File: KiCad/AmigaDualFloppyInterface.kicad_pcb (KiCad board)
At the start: 2 copper layers, 62 x 69 mm, 21 parts, among them J1 Floppy Power In, J2 Floppy B, J3 Motherboard, J4 Floppy Power Out, J5 Floppy A, J6 Conn_01x02_Pin, J7 Conn_01x02_Pin, U1 74LS38, U2 74LS74, U3 74LS157

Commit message: Fix project footprint library
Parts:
- removed the OSHW at (60.0, 128.0)
- added OSHW: LOGO, MyFootprints:OSHW_logo, F.Cu at (60.0, 128.0)

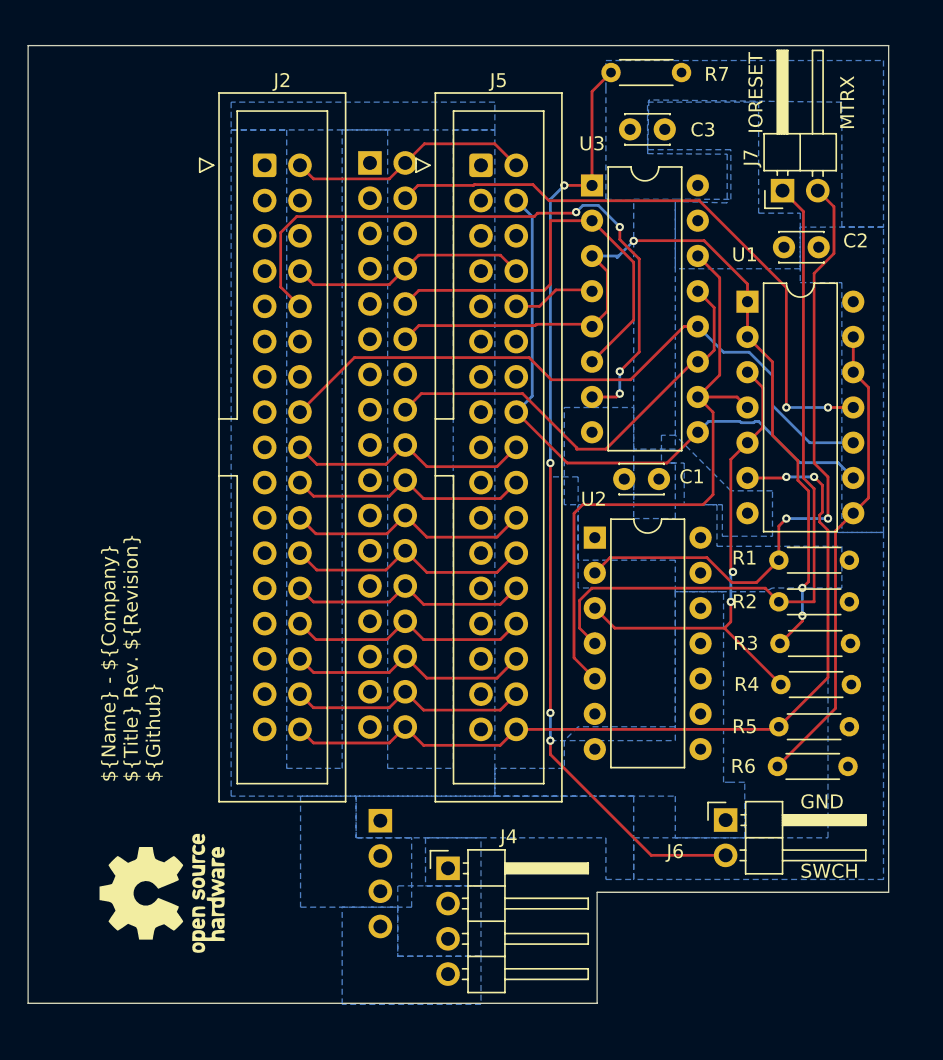
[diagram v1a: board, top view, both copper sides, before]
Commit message: Add files via upload
Updated design with separate df1 LED
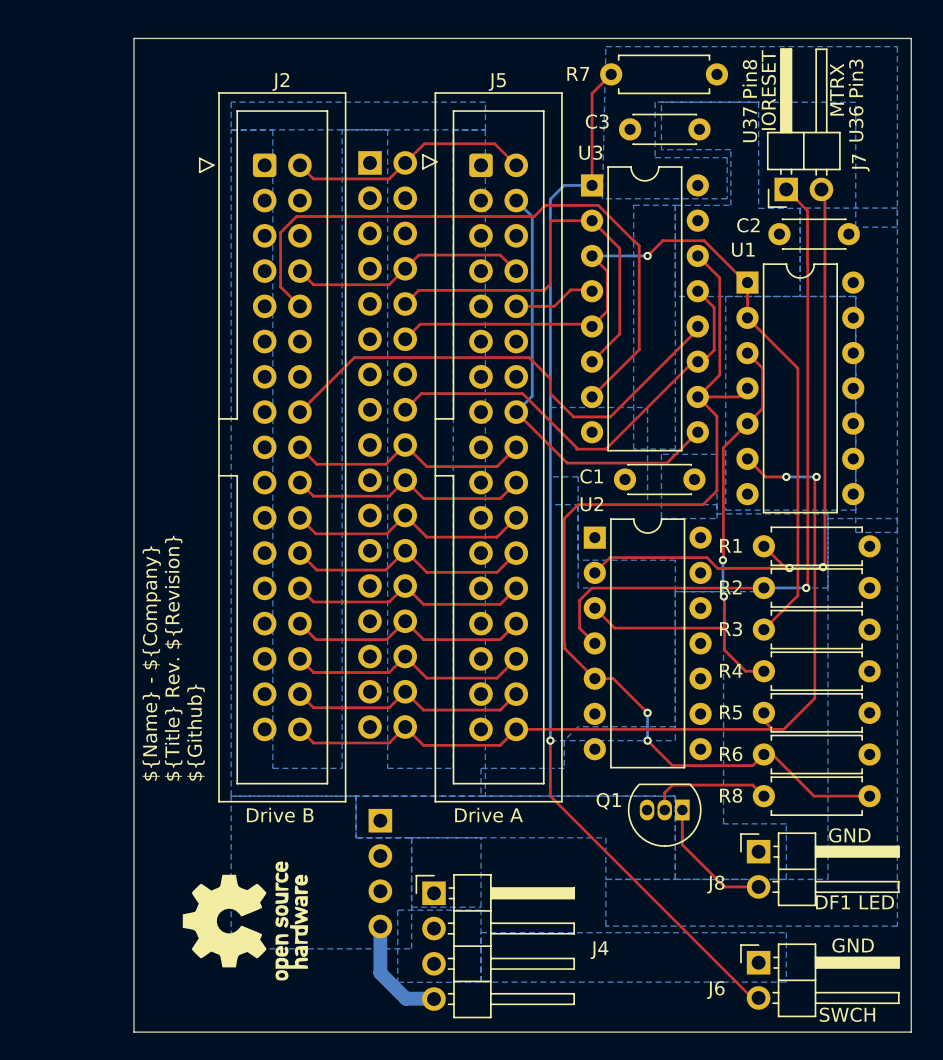
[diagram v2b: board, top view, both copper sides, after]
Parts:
- added J8: DF1 Activity, Connector_PinHeader_2.54mm:PinHeader_1x02_P2.54mm_Horizontal, F.Cu at (103.0, 125.0)
- added Q1: 2N3906, Package_TO_SOT_THT:TO-92_Inline, F.Cu at (97.5, 122.0)
- added R8: 4.7k, Resistor_THT:R_Axial_DIN0207_L6.3mm_D2.5mm_P7.62mm_Horizontal, F.Cu at (111.0, 121.0)
- C1, C2, C3: footprint Capacitor_THT:C_Disc_D3.0mm_W2.0mm_P2.50mm -> Capacitor_THT:C_Disc_D4.3mm_W1.9mm_P5.00mm
- J6: value Conn_01x02_Pin -> Drive Switch
- R1, R2, R3, R4, R5, R7: footprint Resistor_THT:R_Axial_DIN0204_L3.6mm_D1.6mm_P5.08mm_Horizontal -> Resistor_THT:R_Axial_DIN0207_L6.3mm_D2.5mm_P7.62mm_Horizontal
- R6: value 1k -> 10k; footprint Resistor_THT:R_Axial_DIN0204_L3.6mm_D1.6mm_P5.08mm_Horizontal -> Resistor_THT:R_Axial_DIN0207_L6.3mm_D2.5mm_P7.62mm_Horizontal
- moved J6 10.5 mm to (103.0, 133.0)
- moved OSHW 6.32 mm to (66.0, 130.0)
- moved C1 2.56 mm to (98.4, 98.2)
- moved R7 2.56 mm to (100.0, 69.0)
- moved C2 2.37 mm to (109.5, 80.5)
- moved J4 2.06 mm to (79.6, 128.0)
- moved R6 1.78 mm to (111.0, 118.0)
- moved R1 1.77 mm to (111.0, 103.0)
- moved R2 1.77 mm to (111.0, 106.0)
- moved R5 1.77 mm to (111.0, 115.0)
- moved R3 1.70 mm to (111.0, 109.0)
- moved R4 1.63 mm to (111.0, 112.0)
- moved U1 1.38 mm to (102.2, 84.0)
- moved J7 0.28 mm to (105.0, 77.3)
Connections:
- J3 pad 4: ~{INUSE} -> unconnected-(J3-Pin_4-Pad4)
- R6 pad 2: Net-(R6-Pad2) -> /~{MTR1}
- U1 pad 10: ~{MTRB} -> GND
- U1 pad 11: ~{INUSE} -> unconnected-(U1-Pad11)
- U1 pad 12: Net-(R6-Pad2) -> GND
- U1 pad 13: Net-(R6-Pad2) -> GND
- U1 pad 8: Net-(R6-Pad2) -> unconnected-(U1-Pad8)
- U1 pad 9: ~{MTRA} -> GND
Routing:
- net ~{INUSE}: track 44.4 -> 0.00 mm, vias 2 -> 0
- net Net-(R6-Pad2): track 34.1 -> 0.00 mm
- net /~{MTR1}: track 46.0 -> 72.1 mm, vias 0 -> 2
- net ~{MTRA}: track 45.0 -> 31.7 mm
- net ~{MTRB}: track 48.5 -> 35.5 mm
- net Net-(J8-Pin_2): track 0.00 -> 9.26 mm
- net Net-(Q1-B): track 0.00 -> 8.95 mm
- net /SWCH: track 67.8 -> 76.0 mm, vias 4 -> 1
- net /+12V: track 0.00 -> 8.00 mm
- net /~{IORESET}: track 51.8 -> 49.7 mm, vias 0 -> 1
- net ~{SEL1}: track 61.8 -> 60.4 mm, vias 3 -> 1
- net ~{SELB}: track 47.3 -> 46.0 mm, vias 4 -> 0
- net ~{RDY}: track 61.8 -> 62.9 mm
- net ~{SEL0}: track 31.3 -> 30.4 mm
- net /~{MTRX}: track 46.5 -> 47.1 mm
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- removed copper zone on B.Cu, net /+12V
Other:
- board size 62 x 69 mm -> 56 x 71.6 mm
- board text added: "${Name} - ${Company} ${Title} Rev. ${REVISION} ${Github}"
- board text added: "DF1 LED"
- board text added: "Drive A"
- board text added: "Drive B"
- board text added: "U36 Pin3"
- board text added: "U37 Pin8"
- board text removed: "${Name} - ${Company} ${Title} Rev. ${Revision} ${Github}"
